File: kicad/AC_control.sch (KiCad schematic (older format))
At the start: 13 parts, among them CN2 220Vin, CN3 Trasf, U2 Opto TRIAC Dip6, U3 TLP672-2

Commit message: Schematic update
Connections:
- net labels added: TRIAC
- net labels removed: RB1
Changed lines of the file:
@@
 LIBS:power
 LIBS:device
-LIBS:transistors
-LIBS:conn
 LIBS:linear
 LIBS:regul
-LIBS:74xx
-LIBS:cmos4000
 LIBS:adc-dac
 LIBS:memory
@@
 LIBS:digital-audio
 LIBS:philips
-LIBS:display
 LIBS:cypress
 LIBS:siliconi
@@
 LIBS:atmel
 LIBS:contrib
-LIBS:valves
 LIBS:w_connectors
 LIBS:max6675
 LIBS:lcd16x2
-LIBS:switches
 LIBS:HotAirGun-cache
 EELAYER 26 0
@@
 220N
 Text GLabel 3680 4240 0    60   Input ~ 0
-RB1
+TRIAC
 Text GLabel 7230 3740 2    60   Input ~ 0
 220F

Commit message: Modified the Kicad schematic adding the reset to I2c controller
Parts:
- U2: symbol MOC3032M -> MOC3032M-RESCUE-HotAirGun
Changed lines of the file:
@@
-EESchema Schematic File Version 3
+EESchema Schematic File Version 2
 LIBS:HotAirGun-rescue
 LIBS:power
 LIBS:device
+LIBS:transistors
+LIBS:conn
 LIBS:linear
 LIBS:regul
+LIBS:74xx
+LIBS:cmos4000
 LIBS:adc-dac
 LIBS:memory
@@
 LIBS:digital-audio
 LIBS:philips
+LIBS:display
 LIBS:cypress
 LIBS:siliconi
@@
 LIBS:atmel
 LIBS:contrib
-LIBS:w_connectors
+LIBS:valves
 LIBS:max6675
 LIBS:lcd16x2
+LIBS:switches
 LIBS:HotAirGun-cache
-EELAYER 26 0
+EELAYER 25 0
 EELAYER END
 $Descr A4 11693 8268
@@
 $EndComp
 $Comp
-L MOC3032M U2
+L MOC3032M-RESCUE-HotAirGun U2
 U 1 1 59BB46B7
 P 4530 4340

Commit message: added step-down circuit
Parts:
- added F2: 2A, symbol Fuse
- L1: value ~ -> 100uH
- R18: value ~ -> 330R
- U2: value Opto TRIAC Dip6 -> ~
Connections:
- wire segments 31 -> 29
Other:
- note added: "Alimentatore"
- note added: "Rete 200V"
- moved on the sheet: CN1, R17, R18, R19, R20, TR1
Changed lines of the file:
@@
 $EndDescr
 Wire Wire Line
-	5680 4080 5680 4190
-Wire Wire Line
-	5230 3530 5230 3640
-Wire Wire Line
-	5680 3530 5680 3780
-Wire Wire Line
-	5580 4690 5830 4690
-Wire Wire Line
-	5680 4590 5680 4490
-Wire Wire Line
-	5830 4590 5680 4590
-Wire Wire Line
-	4830 4440 5530 4440
-Wire Wire Line
-	5230 4240 5230 3940
-Wire Wire Line
-	4830 4240 5230 4240
-Wire Wire Line
-	3680 4240 3830 4240
-Wire Wire Line
-	4130 4240 4230 4240
-Wire Wire Line
-	4130 4440 4230 4440
+	4120 4960 4120 5070
+Wire Wire Line
+	4020 5570 4270 5570
+Wire Wire Line
+	4120 5470 4120 5370
+Wire Wire Line
+	4270 5470 4120 5470
+Wire Wire Line
+	3270 5320 3970 5320
+Wire Wire Line
+	2120 5120 2270 5120
+Wire Wire Line
+	2570 5120 2670 5120
+Wire Wire Line
+	2570 5320 2670 5320
 Wire Wire Line
 	6880 3740 7230 3740
@@
 	6880 4190 7780 4190
 Wire Wire Line
-	7030 2650 6930 2650
-Wire Wire Line
-	7430 2650 7330 2650
-Wire Wire Line
-	7130 2850 6930 2850
-Wire Wire Line
-	5380 2250 5380 2750
-Wire Wire Line
-	4580 2250 5380 2250
-Wire Wire Line
-	4580 2750 4780 2750
-Wire Wire Line
-	5680 3050 5080 3050
-Wire Wire Line
-	5680 2850 5680 3050
-Wire Wire Line
-	6080 2650 6130 2650
-Wire Wire Line
-	5680 2650 5780 2650
-Wire Wire Line
-	5680 2450 5680 2650
-Wire Wire Line
-	5080 2450 5680 2450
-Connection ~ 5680 3530
-Wire Wire Line
-	5230 3530 5880 3530
-Wire Wire Line
-	6130 2850 5680 2850
-Text GLabel 5880 3530 2    60   Input ~ 0
-220F
-Text GLabel 5580 4690 0    60   Input ~ 0
-220N
-Text GLabel 3680 4240 0    60   Input ~ 0
+	4730 1990 4630 1990
+Wire Wire Line
+	5130 1990 5030 1990
+Wire Wire Line
+	4830 2190 4630 2190
+Wire Wire Line
+	3080 1590 3080 2090
+Wire Wire Line
+	2280 1590 3080 1590
+Wire Wire Line
+	2280 2090 2480 2090
+Wire Wire Line
+	3380 2390 2780 2390
+Wire Wire Line
+	3380 2190 3380 2390
+Wire Wire Line
+	3780 1990 3830 1990
+Wire Wire Line
+	3380 1990 3480 1990
+Wire Wire Line
+	3380 1790 3380 1990
+Wire Wire Line
+	2780 1790 3380 1790
+Wire Wire Line
+	3830 2190 3380 2190
+Text GLabel 3680 3820 1    60   Input ~ 0
+220F
+Text GLabel 4020 5570 0    60   Input ~ 0
+220N
+Text GLabel 2120 5120 0    60   Input ~ 0
 TRIAC
 Text GLabel 7230 3740 2    60   Input ~ 0
@@
 Text GLabel 7480 4090 2    60   Input ~ 0
 220F
-Text GLabel 7430 2650 2    60   Input ~ 0
+Text GLabel 5130 1990 2    60   Input ~ 0
 FASE_0
 $Comp
 L R R20
 U 1 1 59BB469A
-P 7180 2650
-F 0 "R20" V 7260 2650 50  0000 C CNN
-F 1 "220R" V 7180 2650 50  0000 C CNN
-F 2 "" V 7110 2650 50  0000 C CNN
-F 3 "" H 7180 2650 50  0000 C CNN
-	1    7180 2650
-	0    1    1    0
-$EndComp
-$Comp
-L GND #PWR?
+P 4880 1990
+F 0 "R20" V 4960 1990 50  0000 C CNN
+F 1 "220R" V 4880 1990 50  0000 C CNN
+F 2 "" V 4810 1990 50  0000 C CNN
+F 3 "" H 4880 1990 50  0000 C CNN
+	1    4880 1990
+	0    1    1    0
+$EndComp
+$Comp
+L GND #PWR21
 U 1 1 59BB46A1
-P 7130 2850
-F 0 "#PWR?" H 7130 2600 50  0001 C CNN
-F 1 "GND" H 7130 2700 50  0000 C CNN
-F 2 "" H 7130 2850 50  0000 C CNN
-F 3 "" H 7130 2850 50  0000 C CNN
-	1    7130 2850
+P 4830 2190
+F 0 "#PWR21" H 4830 1940 50  0001 C CNN
+F 1 "GND" H 4830 2040 50  0000 C CNN
+F 2 "" H 4830 2190 50  0000 C CNN
+F 3 "" H 4830 2190 50  0000 C CNN
+	1    4830 2190
 	0    -1   -1   0
 $EndComp
-Text GLabel 4580 2250 0    60   Input ~ 0
-220N
-Text GLabel 4580 2750 0    60   Input ~ 0
+Text GLabel 2280 1590 0    60   Input ~ 0
+220N
+Text GLabel 2280 2090 0    60   Input ~ 0
 220F
 $Comp
@@
 L MOC3032M-RESCUE-HotAirGun U2
 U 1 1 59BB46B7
-P 4530 4340
-F 0 "U2" H 4330 4540 50  0000 L CNN
-F 1 "Opto TRIAC Dip6" H 4230 4140 50  0000 L CNN
-F 2 "" H 4330 4140 50  0000 L CIN
-F 3 "" H 4495 4340 50  0000 L CNN
-	1    4530 4340
+P 2970 5220
+F 0 "U2" H 2770 5420 50  0000 L CNN
+F 1 "~" H 2670 5020 50  0000 L CNN
+F 2 "" H 2770 5020 50  0000 L CIN
+F 3 "MOC3023" H 2770 5030 50  0000 L CNN
+	1    2970 5220
 	1    0    0    -1
 $EndComp
@@
 L TLP627-2 U3
 U 1 1 59BB46BE
-P 6530 2750
-F 0 "U3" H 6520 3050 60  0000 L BNN
-F 1 "TLP672-2" H 2630 -4400 60  0001 C CNN
-F 2 "" H 2630 -4400 60  0001 C CNN
-F 3 "" H 2630 -4400 60  0001 C CNN
-	1    6530 2750
+P 4230 2090
+F 0 "U3" H 4220 2390 60  0000 L BNN
+F 1 "TLP672-2" H 330 -5060 60  0001 C CNN
+F 2 "" H 330 -5060 60  0001 C CNN
+F 3 "" H 330 -5060 60  0001 C CNN
+	1    4230 2090
 	1    0    0    -1
 $EndComp
@@
 L CONN_01X02 CN1
 U 1 1 59BB46CC
-P 6030 4640
-F 0 "CN1" H 6030 4640 60  0000 L BNN
-F 1 "~" H 2730 -4660 60  0001 C CNN
-F 2 "" H 2730 -4660 60  0001 C CNN
-F 3 "" H 2730 -4660 60  0001 C CNN
-	1    6030 4640
+P 4470 5520
+F 0 "CN1" H 4470 5520 60  0000 L BNN
+F 1 "~" H 1170 -3780 60  0001 C CNN
+F 2 "" H 1170 -3780 60  0001 C CNN
+F 3 "" H 1170 -3780 60  0001 C CNN
+	1    4470 5520
 	1    0    0    -1
 $EndComp
@@
 L R R18
 U 1 1 59BB46D3
-P 5230 3790
-F 0 "R18" V 5310 3790 50  0000 C CNN
-F 1 "~" V 5230 3790 50  0000 C CNN
-F 2 "" V 5160 3790 50  0000 C CNN
-F 3 "" H 5230 3790 50  0000 C CNN
-	1    5230 3790
+P 3680 4810
+F 0 "R18" V 3760 4810 50  0000 C CNN
+F 1 "330R" V 3680 4810 50  0000 C CNN
+F 2 "" V 3610 4810 50  0000 C CNN
+F 3 "" H 3680 4810 50  0000 C CNN
+	1    3680 4810
 	1    0    0    -1
 $EndComp
@@
 L R R17
 U 1 1 59BB46DA
-P 3980 4240
-F 0 "R17" V 4060 4240 50  0000 C CNN
-F 1 "330R" V 3980 4240 50  0000 C CNN
-F 2 "" V 3910 4240 50  0000 C CNN
-F 3 "" H 3980 4240 50  0000 C CNN
-	1    3980 4240
+P 2420 5120
+F 0 "R17" V 2340 5080 50  0000 C CNN
+F 1 "330R" V 2420 5120 50  0000 C CNN
+F 2 "" V 2350 5120 50  0000 C CNN
+F 3 "" H 2420 5120 50  0000 C CNN
+	1    2420 5120
 	0    1    1    0
 $EndComp
@@
 L Q_TRIAC_AAG TR1
 U 1 1 59BB46E1
-P 5680 4340
-F 0 "TR1" H 5730 4390 50  0000 L CNN
-F 1 "~" H 2655 -4660 50  0000 L CNN
-F 2 "" V 2605 -4585 50  0001 C CNN
-F 3 "" V 2530 -4610 50  0001 C CNN
-	1    5680 4340
+P 4120 5220
+F 0 "TR1" H 4170 5270 50  0000 L CNN
+F 1 "~" H 1095 -3780 50  0000 L CNN
+F 2 "" V 1045 -3705 50  0001 C CNN
+F 3 "" V 970 -3730 50  0001 C CNN
+	1    4120 5220
 	1    0    0    -1
 $EndComp
@@
 L L_Core_Iron L1
 U 1 1 59BB46E8
-P 5680 3930
-F 0 "L1" V 5630 3930 50  0000 C CNN
-F 1 "~" V 5780 3930 50  0000 C CNN
-F 2 "" H 5680 3930 50  0000 C CNN
-F 3 "" H 5680 3930 50  0000 C CNN
-	1    5680 3930
+P 4120 4810
+F 0 "L1" V 4070 4810 50  0000 C CNN
+F 1 "100uH" V 4220 4810 50  0000 C CNN
+F 2 "" H 4120 4810 50  0000 C CNN
+F 3 "" H 4120 4810 50  0000 C CNN
+	1    4120 4810
 	-1   0    0    1
 $EndComp
@@
 L R R19
 U 1 1 59BB46EF
-P 5930 2650
-F 0 "R19" V 6010 2650 50  0000 C CNN
-F 1 "56K" V 5930 2650 50  0000 C CNN
-F 2 "" V 5860 2650 50  0000 C CNN
-F 3 "" H 5930 2650 50  0000 C CNN
-	1    5930 2650
+P 3630 1990
+F 0 "R19" V 3710 1990 50  0000 C CNN
+F 1 "56K" V 3630 1990 50  0000 C CNN
+F 2 "" V 3560 1990 50  0000 C CNN
+F 3 "" H 3630 1990 50  0000 C CNN
+	1    3630 1990
 	0    1    1    0
 $EndComp
@@
 L D_Bridge_+AA- PR1
 U 1 1 59BB46F6
-P 5080 2750
-F 0 "PR1" V 5430 3000 50  0000 C CNN
-F 1 "PontRaddr 2A" V 4850 2480 50  0000 C CNN
-F 2 "" H 5080 2750 50  0000 C CNN
-F 3 "" H 5080 2750 50  0000 C CNN
-	1    5080 2750
+P 2780 2090
+F 0 "PR1" V 3130 2340 50  0000 C CNN
+F 1 "PontRaddr 2A" V 2550 1820 50  0000 C CNN
+F 2 "" H 2780 2090 50  0000 C CNN
+F 3 "" H 2780 2090 50  0000 C CNN
+	1    2780 2090
 	0    -1   -1   0
 $EndComp
 $Comp
-L GND #GND_06
+L GND #GND_6
 U 1 1 59BB46FD
-P 4130 4440
-F 0 "#GND_06" H 4130 4190 50  0001 C CNN
-F 1 "GND" H 4130 4290 50  0000 C CNN
-F 2 "" H 4130 4440 50  0000 C CNN
-F 3 "" H 4130 4440 50  0000 C CNN
-	1    4130 4440
-	0    1    1    0
-$EndComp
-Text Notes 5530 3250 0    60   ~ 0
+P 2570 5320
+F 0 "#GND_6" H 2570 5070 50  0001 C CNN
+F 1 "GND" H 2570 5170 50  0000 C CNN
+F 2 "" H 2570 5320 50  0000 C CNN
+F 3 "" H 2570 5320 50  0000 C CNN
+	1    2570 5320
+	0    1    1    0
+$EndComp
+Text Notes 3340 1280 0    60   ~ 0
 Controllo Fase
+$Comp
+L Fuse F2
+U 1 1 59F9A7EE
+P 3680 3970
+F 0 "F2" V 3750 3970 50  0000 C CNN
+F 1 "2A" V 3610 3970 50  0000 C CNN
+F 2 "" H 3680 3970 50  0000 C CNN
+F 3 "" H 3680 3970 50  0000 C CNN
+	1    3680 3970
+	-1   0    0    1
+$EndComp
+Text Notes 6160 3710 0    60   ~ 0
+Rete 200V
+Text Notes 6040 4120 0    60   ~ 0
+Alimentatore
+Wire Wire Line
+	3270 5120 3680 5120
+Wire Wire Line
+	3680 5120 3680 4960
+Wire Wire Line
+	3680 4660 4120 4660
 $EndSCHEMATC

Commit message: Update the schematic with the safety relays for 220V. Microcontroller page now is connect with the grid.
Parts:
- removed CN1: ~, symbol CONN_01X02
- removed L1: 100uH, symbol L_Core_Iron
- removed TR1: ~, symbol Q_TRIAC_AAG
- removed U2: ~, symbol MOC3032M-RESCUE-HotAirGun
- added D3: Q_TRIAC_AAG, symbol Q_TRIAC_AAG
- added D4: LED, symbol LED
- added J7: Screw_Terminal_1x02, symbol Screw_Terminal_1x02
- added L1: L_Core_Ferrite, symbol L_Core_Ferrite
- added Q3: Q_PNP_CBE, symbol Q_PNP_CBE
- added R21: 330R, symbol R
- added R22: 470R, symbol R
- added RL?: FINDER-40.52, symbol FINDER-40.52
- added U2: MOC3023M, DIP-6, symbol MOC3023M
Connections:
- net labels added: +5V, RELE_SIC_220V
- wire segments 29 -> 36
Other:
- moved on the sheet: F2, R18

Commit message: Reduce some pic resolution. Update PDF schematic.
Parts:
- gave numbers to parts that had none: 1
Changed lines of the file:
@@
 $EndComp
 $Comp
-L GND #PWR23
+L GND #PWR032
 U 1 1 59BB46A1
 P 4830 2190
-F 0 "#PWR23" H 4830 1940 50  0001 C CNN
+F 0 "#PWR032" H 4830 1940 50  0001 C CNN
 F 1 "GND" H 4830 2040 50  0000 C CNN
 F 2 "" H 4830 2190 50  0000 C CNN
@@
 TRIAC
 $Comp
-L GND #PWR21
+L GND #PWR033
 U 1 1 5A0A68C0
 P 2000 6050
-F 0 "#PWR21" H 2000 5800 50  0001 C CNN
+F 0 "#PWR033" H 2000 5800 50  0001 C CNN
 F 1 "GND" H 2000 5900 50  0000 C CNN
 F 2 "" H 2000 6050 50  0000 C CNN
@@
 	1300 5850 1450 5850
 $Comp
-L +5V #PWR22
+L +5V #PWR034
 U 1 1 5A0A6B0B
 P 3300 4400
-F 0 "#PWR22" H 3300 4250 50  0001 C CNN
+F 0 "#PWR034" H 3300 4250 50  0001 C CNN
 F 1 "+5V" H 3300 4540 50  0000 C CNN
 F 2 "" H 3300 4400 50  0000 C CNN
@@
 $EndComp
 $Comp
-L GND #PWR24
+L GND #PWR035
 U 1 1 5A0A73FA
 P 3750 5600
-F 0 "#PWR24" H 3750 5350 50  0001 C CNN
+F 0 "#PWR035" H 3750 5350 50  0001 C CNN
 F 1 "GND" H 3750 5450 50  0000 C CNN
 F 2 "" H 3750 5600 50  0000 C CNN
@@
 $EndComp
 $Comp
-L FINDER-40.52 RL?
+L FINDER-40.52 RL1
 U 1 1 5A0A81E7
 P 3100 4900
-F 0 "RL?" H 3950 5050 50  0000 L CNN
+F 0 "RL1" H 3950 5050 50  0000 L CNN
 F 1 "FINDER-40.52" H 3950 4950 50  0000 L CNN
 F 2 "" H 3100 4900 50  0000 C CNN

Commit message: v2
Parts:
- removed CN2: 220Vin, symbol CONN_01X02
- removed CN3: Trasf, symbol CONN_01X02
- removed F1: Fuse1, symbol Fuse
- removed PR1: PontRaddr 2A, symbol D_Bridge_+AA-
- removed R19: 56K, symbol R
- removed R20: 220R, symbol R
- removed U3: TLP672-2, symbol TLP627-2
- added D3: D_Bridge_+-AA, Msystem:Diode_Bridge_8.5, symbol D_Bridge_+-AA
- added F2: Fuse, Fuse_Holders_and_Fuses:Fuseholder5x20_horiz_open_Schurter_0031_8201, symbol Fuse
- added J5: PWR_IN, Connectors_Phoenix:PhoenixContact_MSTBVA-G_03x5.08mm_Vertical, symbol Screw_Terminal_1x03
- added J6: PWR_Suply, Connectors_Phoenix:PhoenixContact_MSTBVA-G_02x5.08mm_Vertical, symbol Screw_Terminal_1x02
- added R10: 56k, Resistors_THT:R_Axial_DIN0411_L9.9mm_D3.6mm_P15.24mm_Horizontal, symbol R
- added UA1: TLP627, Housings_DIP:DIP-4_W7.62mm, symbol TLP627
- D4: renamed from D3; value Q_TRIAC_AAG -> BTA08; footprint (none) -> TO_SOT_Packages_THT:TO-220_Vertical
- D5: renamed from D4; footprint (none) -> LEDs:LED-3MM
- F1: renamed from F2; footprint (none) -> Fuse_Holders_and_Fuses:Fuseholder5x20_horiz_open_Schurter_0031_8201
- J4: renamed from J7; value Screw_Terminal_1x02 -> HAG Resistor; footprint (none) -> Connectors_Phoenix:PhoenixContact_MSTBVA-G_02x5.08mm_Vertical
- L1: footprint (none) -> Inductors_THT:L_Toroid_Vertical_L16.0mm_W8.0mm_P7.62mm
- Q2: renamed from Q3; footprint (none) -> TO_SOT_Packages_THT:TO-92_Rugged
- R11: renamed from R17; footprint (none) -> Resistors_SMD:R_0603_HandSoldering
- R12: renamed from R18; footprint (none) -> Resistors_THT:R_Axial_DIN0309_L9.0mm_D3.2mm_P12.70mm_Horizontal
- R13: renamed from R21; value 330R -> 2K2; footprint (none) -> Resistors_SMD:R_0603_HandSoldering
- R14: renamed from R22; footprint (none) -> Resistors_SMD:R_0603_HandSoldering
- RL1: footprint (none) -> Msystem:Relay_SPDT_Schrack-RT1_RM5mm
- U2: footprint DIP-6 -> Housings_DIP:DIP-6_W7.62mm; symbol MOC3023M -> MOC3023M-RESCUE-HotAirGun
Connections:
- net labels added: +24V, 0_FASE, Earth, SAFE_REL
- net labels removed: +5V, FASE_0, RELE_SIC_220V
- wire segments 36 -> 24
- no-connect marks 0 -> 2
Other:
- note added: "Zero Crossing Control"
- note removed: "Alimentatore"
- note removed: "Controllo Fase"
- note removed: "Rete 200V"
- moved on the sheet: D4, D5, F1, J4, L1, Q2, R11, R12, R13, R14, RL1

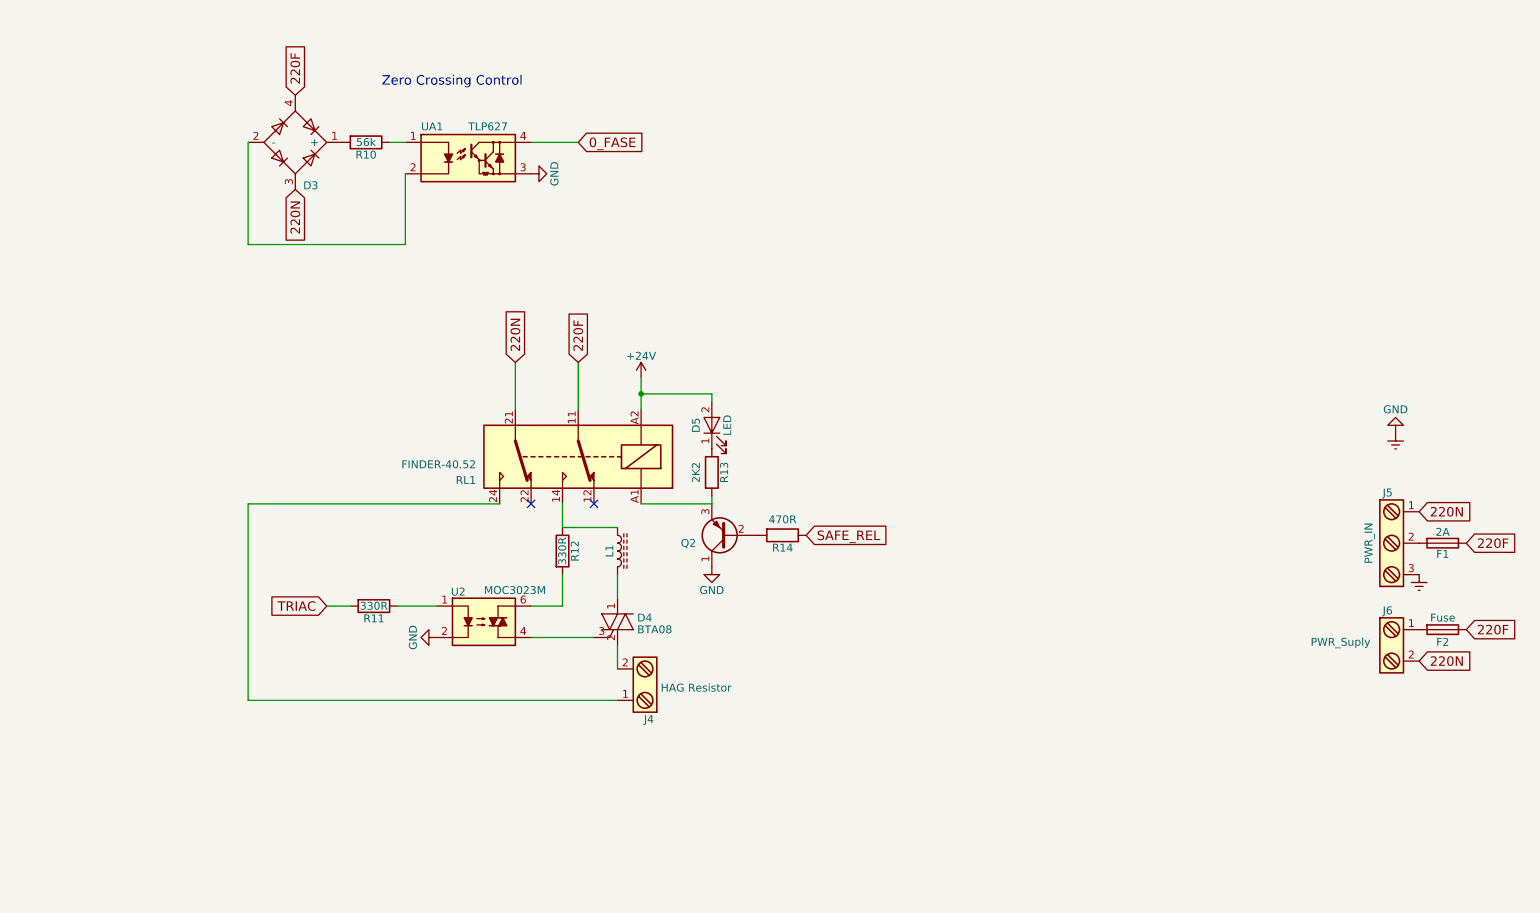
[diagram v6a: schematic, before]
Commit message: New PCB version with smd component Added plot folder with gerber file
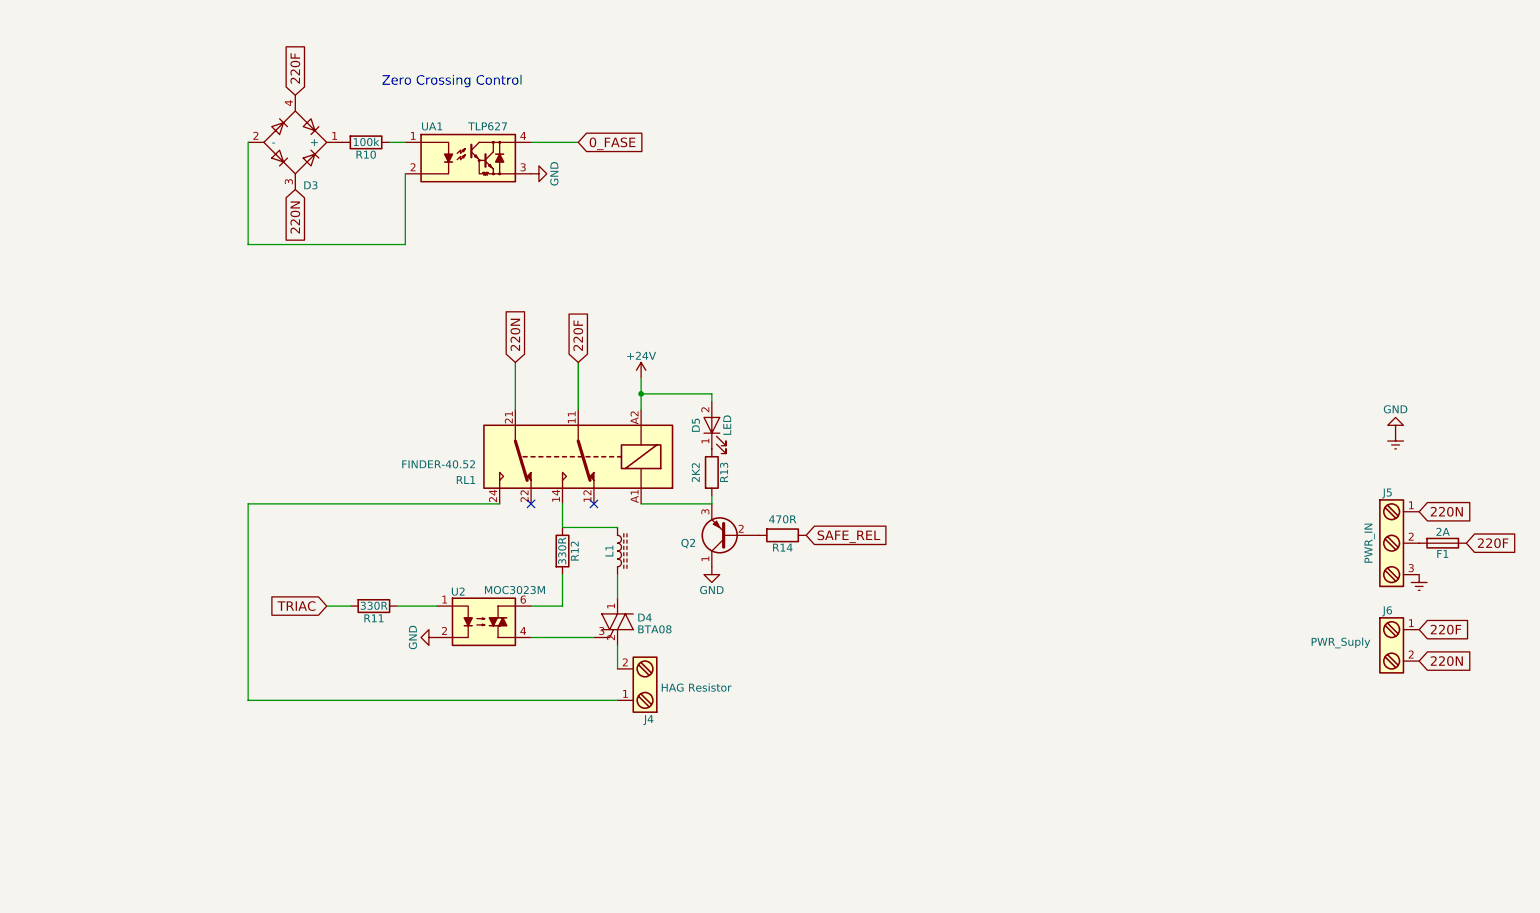
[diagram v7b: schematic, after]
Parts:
- removed F2: Fuse, Fuse_Holders_and_Fuses:Fuseholder5x20_horiz_open_Schurter_0031_8201, symbol Fuse
- R10: value 56k -> 100k
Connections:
- net 220F: now also J6.1
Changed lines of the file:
@@
 	1    0    0    -1
 $EndComp
-$Comp
-L Fuse F2
-U 1 1 5C0721B3
-P 9900 5100
-F 0 "F2" V 9980 5100 50  0000 C CNN
-F 1 "Fuse" V 9825 5100 50  0000 C CNN
-F 2 "Fuse_Holders_and_Fuses:Fuseholder5x20_horiz_open_Schurter_0031_8201" V 9830 5100 50  0001 C CNN
-F 3 "" H 9900 5100 50  0001 C CNN
-	1    9900 5100
-	0    1    1    0
-$EndComp
-Text GLabel 10050 5100 2    60   Input ~ 0
+Text GLabel 9750 5100 2    60   Input ~ 0
 220F
 Text GLabel 9750 5300 2    60   Input ~ 0
@@
 P 3050 2000
 F 0 "R10" V 3130 2000 50  0000 C CNN
-F 1 "56k" V 3050 2000 50  0000 C CNN
+F 1 "100k" V 3050 2000 50  0000 C CNN
 F 2 "Resistors_THT:R_Axial_DIN0411_L9.9mm_D3.6mm_P15.24mm_Horizontal" V 2980 2000 50  0001 C CNN
 F 3 "" H 3050 2000 50  0001 C CNN
